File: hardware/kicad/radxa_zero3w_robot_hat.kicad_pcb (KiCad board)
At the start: 4 copper layers, 65 x 30.9 mm, 127 parts, among them J1 Wago-2, J11 Dynamixel-4, J13 Dynamixel-3, J14 Dynamixel-3, J2 Wago-2, J3 Dynamixel-4, J4 Radxa ZERO 3W 2x20 HAT Header, J5 JST SH, J6 JST SH, J7 JST SH, J8 JST SH, J9 Wago-2, Q1 MMBT3906, Q2 SI2312CDS-T1-GE3, U1 PAM8406D, U10 LM5050-1, U11 BMI088, U2 TLV320AIC3104IRHBR, U3 XC6206P182MR, U4 DNP-CAT24C32HU4, U5 74LVC1G08, U6 SN74LVC1G125DBV, U7 SN74LVC1G126DBVR, U8 SIT3088E, U9 AP63205, Y1 12 MHz

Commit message: [verified] fix(validation): enforce fail-closed strict-port guards
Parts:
- R18, R19: value 0R -> DNP-0R
- R20, R21, R34, R35, R38, R39: value 10k -> DNP-10k
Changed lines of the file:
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@@
 			)
 		)
-		(property "Value" "0R"
+		(property "Value" "DNP-0R"
 			(at 0 1.17 0)
 			(layer "F.Fab")
@@
 		(sheetname "/Schematic/Sensors/")
 		(sheetfile "sensors.kicad_sch")
-		(attr smd)
+		(attr smd dnp)
 		(fp_line
 			(start -0.153641 0.38)
@@
 			)
 		)
-		(property "Value" "10k"
+		(property "Value" "DNP-10k"
 			(at 0 -1.17 90)
 			(layer "B.Fab")
@@
 		(sheetname "/Schematic/Sensors/")
 		(sheetfile "sensors.kicad_sch")
-		(attr smd)
+		(attr smd dnp)
 		(fp_line
 			(start -0.153641 -0.38)
@@
 			)
 		)
-		(property "Value" "10k"
+		(property "Value" "DNP-10k"
 			(at 0 -1.17 90)
 			(layer "B.Fab")
@@
 		(sheetname "/Schematic/Sensors/")
 		(sheetfile "sensors.kicad_sch")
-		(attr smd)
+		(attr smd dnp)
 		(fp_line
 			(start -0.153641 -0.38)
@@
 			)
 		)
-		(property "Value" "10k"
+		(property "Value" "DNP-10k"
 			(at 0 -1.17 90)
 			(layer "B.Fab")
@@
 		(sheetname "/Schematic/Sensors/")
 		(sheetfile "sensors.kicad_sch")
-		(attr smd)
+		(attr smd dnp)
 		(fp_line
 			(start -0.153641 -0.38)
@@
 			)
 		)
-		(property "Value" "10k"
+		(property "Value" "DNP-10k"
 			(at 0 -1.17 90)
 			(layer "B.Fab")
@@
 		(sheetname "/Schematic/Sensors/")
 		(sheetfile "sensors.kicad_sch")
-		(attr smd)
+		(attr smd dnp)
 		(fp_line
 			(start -0.153641 -0.38)
@@
 			)
 		)
-		(property "Value" "0R"
+		(property "Value" "DNP-0R"
 			(at 0 -1.17 0)
 			(layer "B.Fab")
@@
 		(sheetname "/Schematic/Sensors/")
 		(sheetfile "sensors.kicad_sch")
-		(attr smd)
+		(attr smd dnp)
 		(fp_line
 			(start -0.153641 0.38)
@@
 			)
 		)
-		(property "Value" "10k"
+		(property "Value" "DNP-10k"
 			(at 0 -1.17 90)
 			(layer "B.Fab")
@@
 		(sheetname "/Schematic/Sensors/")
 		(sheetfile "sensors.kicad_sch")
-		(attr smd)
+		(attr smd dnp)
 		(fp_line
 			(start -0.153641 -0.38)
@@
 			)
 		)
-		(property "Value" "10k"
+		(property "Value" "DNP-10k"
 			(at 0 -1.17 90)
 			(layer "B.Fab")
@@
 		(sheetname "/Schematic/Sensors/")
 		(sheetfile "sensors.kicad_sch")
-		(attr smd)
+		(attr smd dnp)
 		(fp_line
 			(start -0.153641 -0.38)

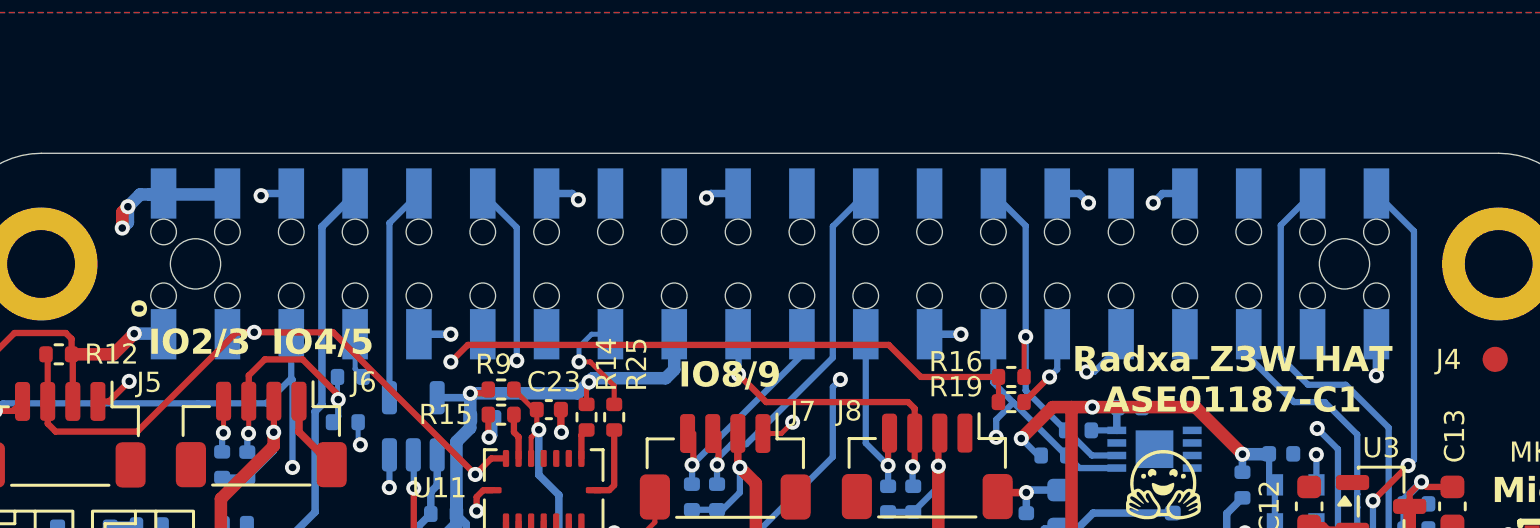
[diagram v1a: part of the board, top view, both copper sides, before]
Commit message: [verified] fix(pcb): qualify J4 pass-through footprint
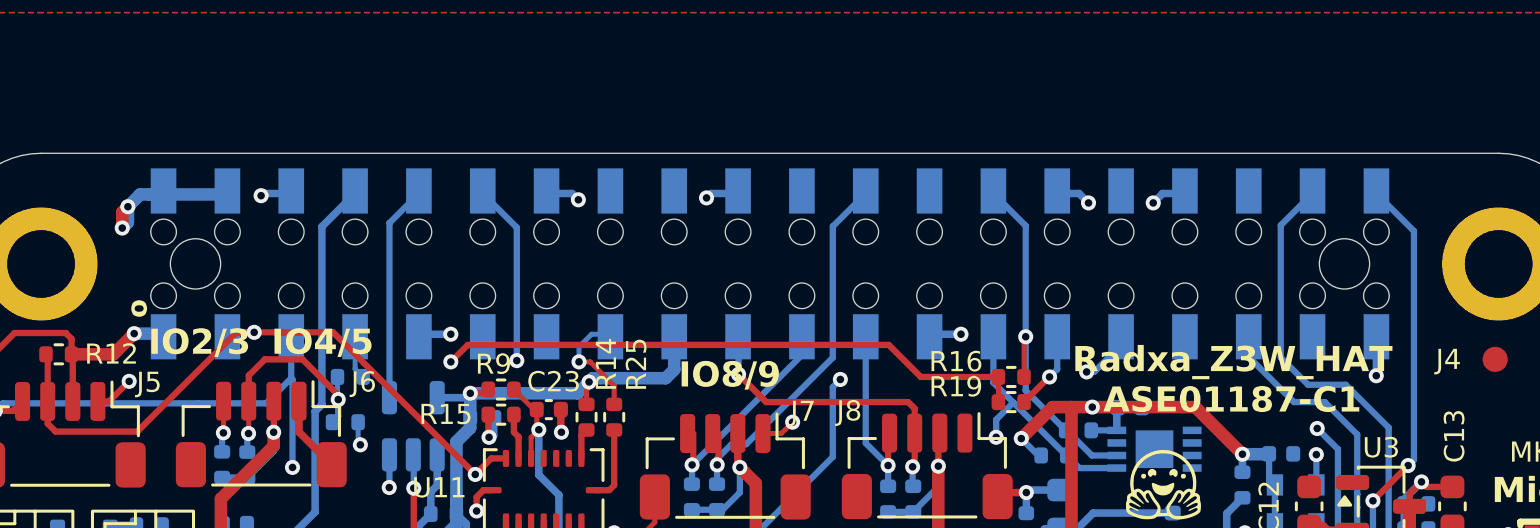
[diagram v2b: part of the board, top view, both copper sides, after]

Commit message: [verified] fix(power): add C45 bypass and mechanical gates
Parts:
- added C45: 10uF 50V X7R, Capacitor_SMD:C_1210_3225Metric, B.Cu at (99.0, 101.0)
- C21, C22: value 22u 6V3 -> 22u 10V
- moved D1 3.66 mm to (99.0, 104.7)
- moved C22 1.84 mm to (95.5, 104.8), turned to 0 degrees
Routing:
- net GND: track 110.7 -> 109.3 mm, vias 38 -> 40
- net +BATT: vias 0 -> 1
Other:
- board text added: "ONE 5V SOURCE ONLY NO USB-C + BATT"
